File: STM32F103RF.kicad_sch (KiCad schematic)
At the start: 57 parts, among them J1 USB_A, J4 Conn_Coaxial, U1 SPX3819M5-L-3-3, U2 STM32F103C6Tx, U3 NRF24L01, Y1 16MHz, Y2 16MHz

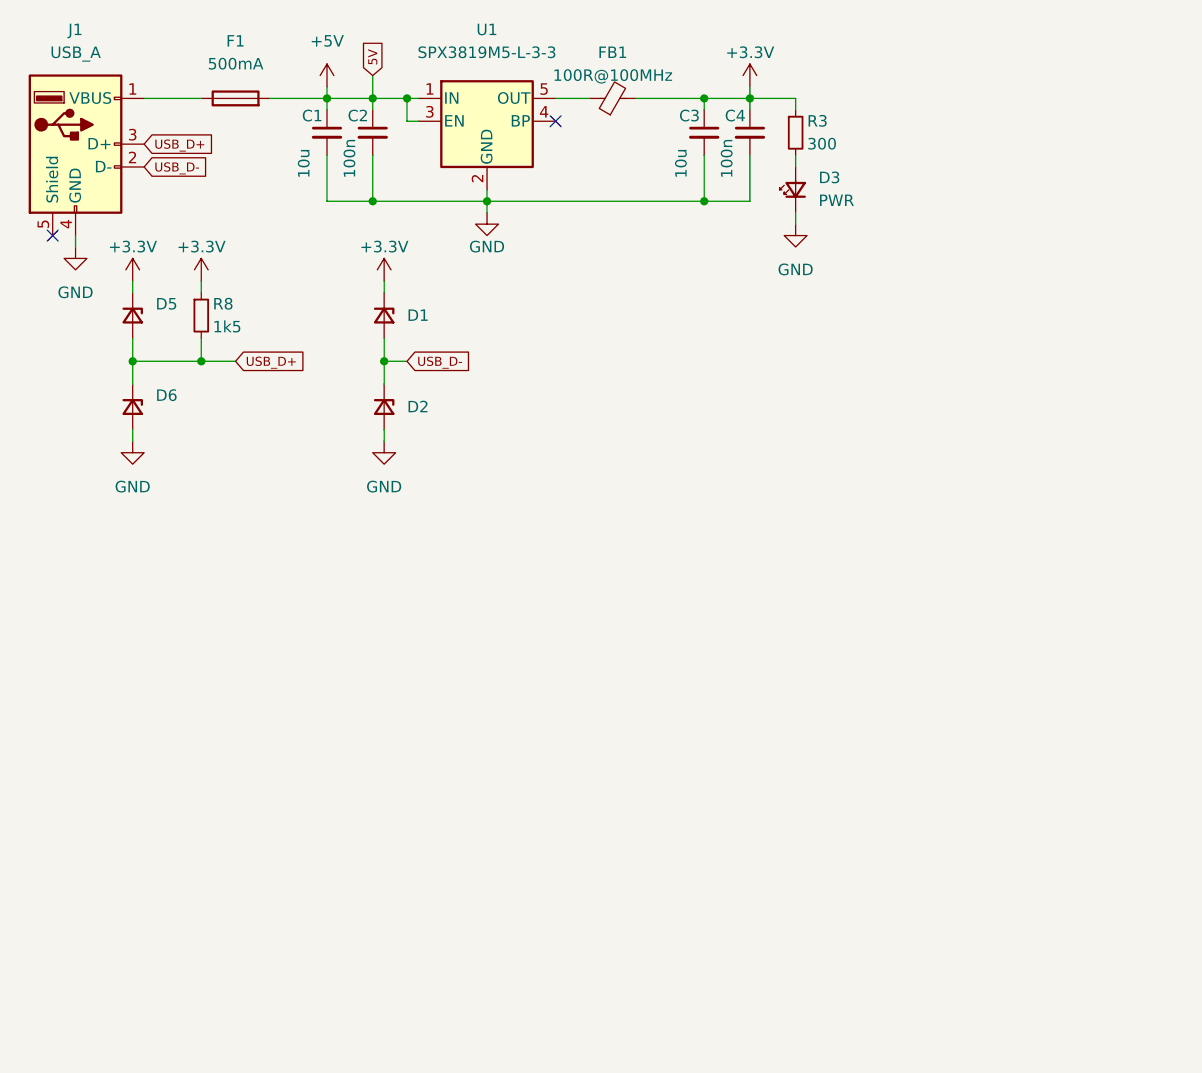
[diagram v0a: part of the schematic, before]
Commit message: Added usbc
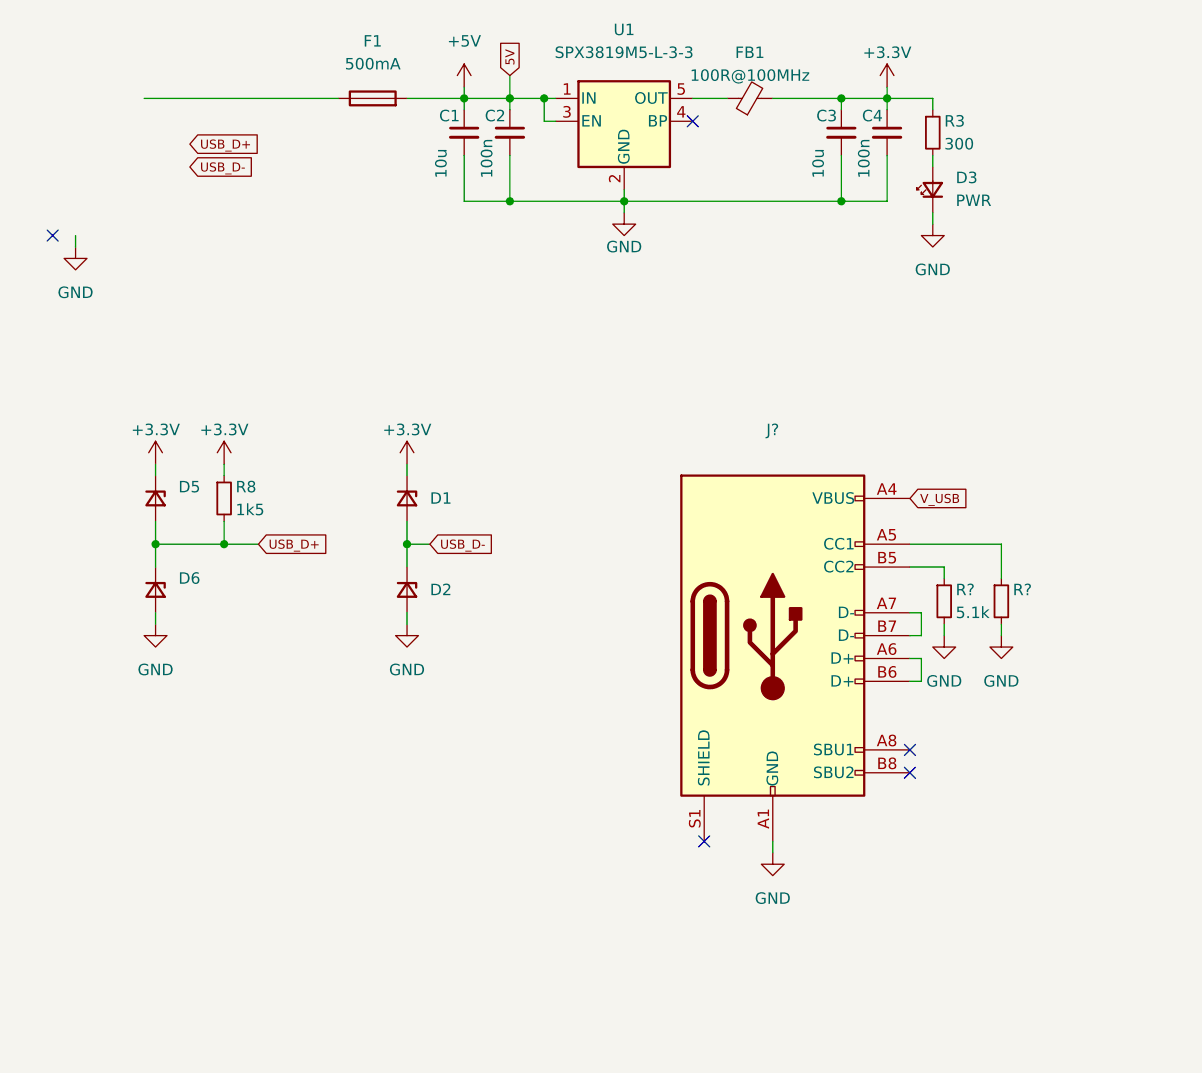
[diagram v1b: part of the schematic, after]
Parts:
- removed J1: USB_A, Connector_USB:USB_A_CNCTech_1001-011-01101_Horizontal, symbol Connector:USB_A
- added J?: (no value), symbol Connector:USB_C_Receptacle_USB2.0
- added R?: 5.1k, Resistor_SMD:R_0603_1608Metric_Pad0.98x0.95mm_HandSolder, symbol Device:R_Small
- added R?: (no value), symbol Device:R_Small
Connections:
- net GND: now also J?.A1 (GND), J?.A12 (GND), J?.B1 (GND), J?.B12 (GND), R?.2, R?.2
- new net: J?.B5 (CC2), R?.1
- new net: J?.A5 (CC1), R?.1
- new net: J?.A6 (D+), J?.B6 (D+)
- new net: J?.A7 (D-), J?.B7 (D-)
- new net V_USB: J?.A4 (VBUS), J?.A9 (VBUS), J?.B4 (VBUS), J?.B9 (VBUS)
- no-connect marks 2 -> 5
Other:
- moved on the sheet: C1, C2, C3, C4, D1, D2, D3, D5, D6, F1, FB1, R3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

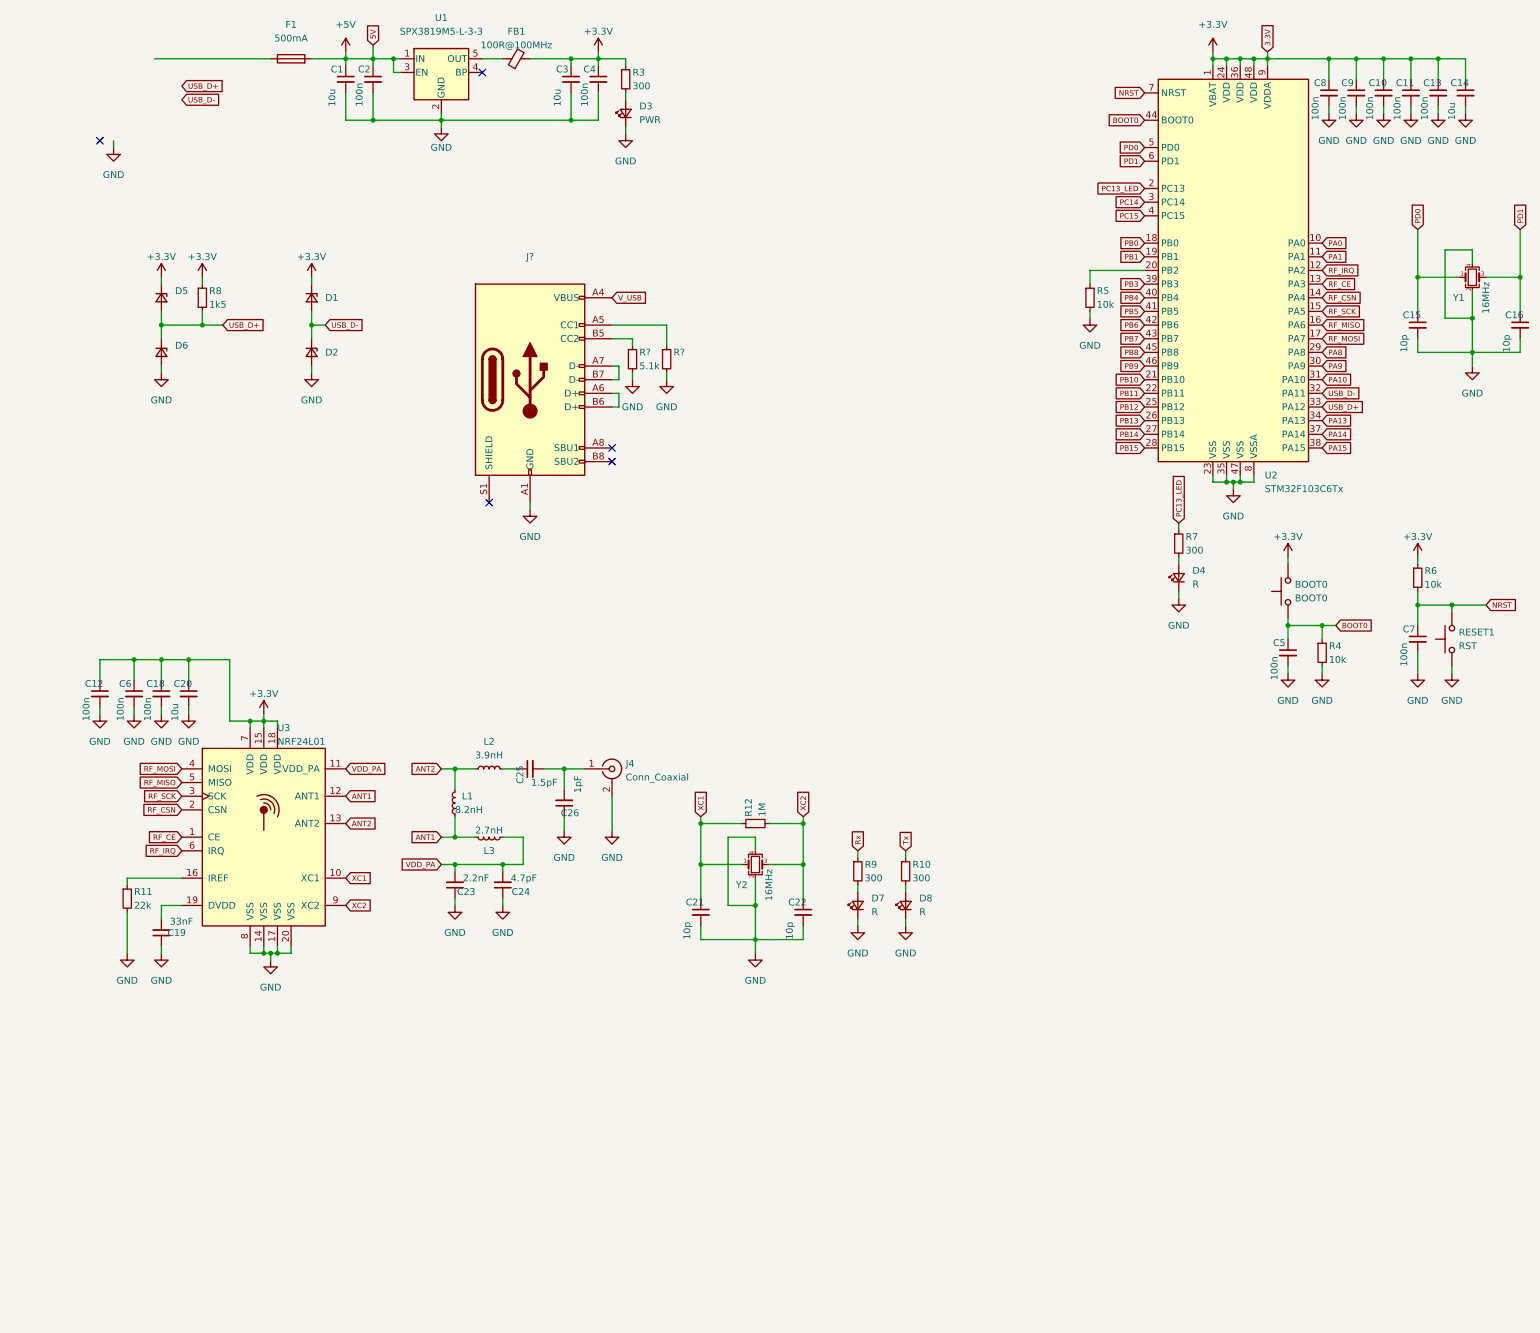
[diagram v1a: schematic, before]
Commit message: placing usb components
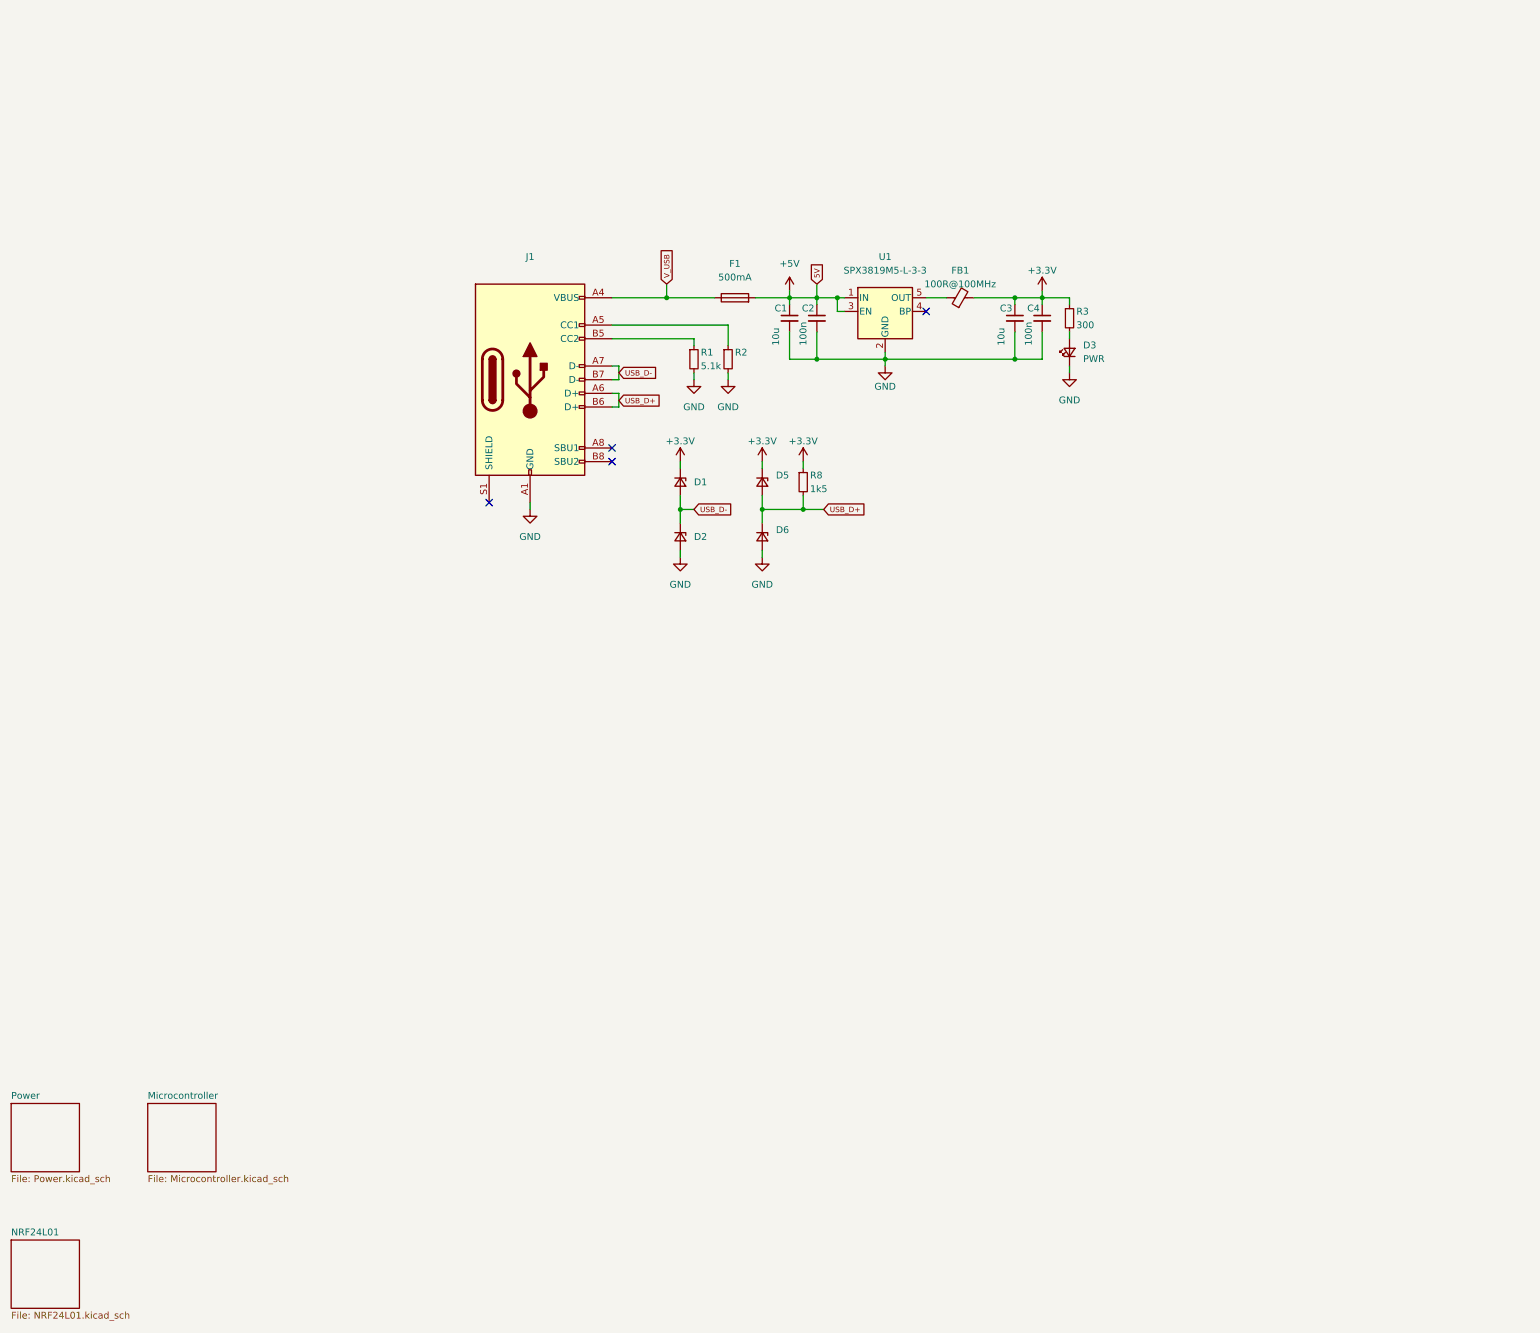
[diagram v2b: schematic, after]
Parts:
- removed BOOT0: BOOT0, Button_Switch_THT:SW_PUSH_6mm, symbol Switch:SW_Push
- removed C10, C11, C12, C13, C18, C5, C6, C7, C8, C9: 100n, Capacitor_SMD:C_0603_1608Metric_Pad1.08x0.95mm_HandSolder, symbol Device:C_Small
- removed C14, C20: 10u, Capacitor_SMD:C_0603_1608Metric_Pad1.08x0.95mm_HandSolder, symbol Device:C_Small
- removed C15, C16, C21, C22: 10p, Capacitor_SMD:C_0603_1608Metric_Pad1.08x0.95mm_HandSolder, symbol Device:C_Small
- removed C19: 33nF, Capacitor_SMD:C_0603_1608Metric_Pad1.08x0.95mm_HandSolder, symbol Device:C_Small
- removed C23: 2.2nF, Capacitor_SMD:C_0603_1608Metric_Pad1.08x0.95mm_HandSolder, symbol Device:C_Small
- removed C24: 4.7pF, Capacitor_SMD:C_0603_1608Metric_Pad1.08x0.95mm_HandSolder, symbol Device:C_Small
- removed C25: 1.5pF, Capacitor_SMD:C_0603_1608Metric_Pad1.08x0.95mm_HandSolder, symbol Device:C_Small
- removed C26: 1pF, Capacitor_SMD:C_0603_1608Metric_Pad1.08x0.95mm_HandSolder, symbol Device:C_Small
- removed D4, D7, D8: R, LED_SMD:LED_0603_1608Metric_Pad1.05x0.95mm_HandSolder, symbol Device:LED_Small
- removed J4: Conn_Coaxial, Connector_Coaxial:SMA_Amphenol_132289_EdgeMount, symbol Connector:Conn_Coaxial
- removed L1: 8.2nH, Inductor_SMD:L_0603_1608Metric_Pad1.05x0.95mm_HandSolder, symbol Device:L_Small
- removed L2: 3.9nH, Inductor_SMD:L_0603_1608Metric_Pad1.05x0.95mm_HandSolder, symbol Device:L_Small
- removed L3: 2.7nH, Inductor_SMD:L_0603_1608Metric_Pad1.05x0.95mm_HandSolder, symbol Device:L_Small
- removed R10, R7, R9: 300, Resistor_SMD:R_0603_1608Metric_Pad0.98x0.95mm_HandSolder, symbol Device:R_Small
- removed R11: 22k, Resistor_SMD:R_0603_1608Metric_Pad0.98x0.95mm_HandSolder, symbol Device:R_Small
- removed R12: 1M, Resistor_SMD:R_0603_1608Metric_Pad0.98x0.95mm_HandSolder, symbol Device:R_Small
- removed R4, R5, R6: 10k, Resistor_SMD:R_0603_1608Metric_Pad0.98x0.95mm_HandSolder, symbol Device:R_Small
- removed RESET1: RST, Button_Switch_THT:SW_PUSH_6mm, symbol Switch:SW_Push
- removed U2: STM32F103C6Tx, Package_QFP:LQFP-48_7x7mm_P0.5mm, symbol MCU_ST_STM32F1:STM32F103C6Tx
- removed U3: NRF24L01, Package_DFN_QFN:QFN-20-1EP_4x4mm_P0.5mm_EP2.5x2.5mm, symbol RF:NRF24L01
- removed Y1, Y2: 16MHz, Crystal:Crystal_SMD_2520-4Pin_2.5x2.0mm, symbol Device:Crystal_GND24_Small
- gave numbers to parts that had none: 3
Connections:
- net USB_D+: now also J1.A6 (D+), J1.B6 (D+)
- net USB_D-: now also J1.A7 (D-), J1.B7 (D-)
- net V_USB: now also F1.1
- no-connect marks 5 -> 4
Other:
- added sheet Microcontroller (Microcontroller.kicad_sch)
- added sheet NRF24L01 (NRF24L01.kicad_sch)
- added sheet Power (Power.kicad_sch)
- moved on the sheet: C1, C2, C3, C4, D1, D2, D3, D5, D6, F1, FB1, R1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

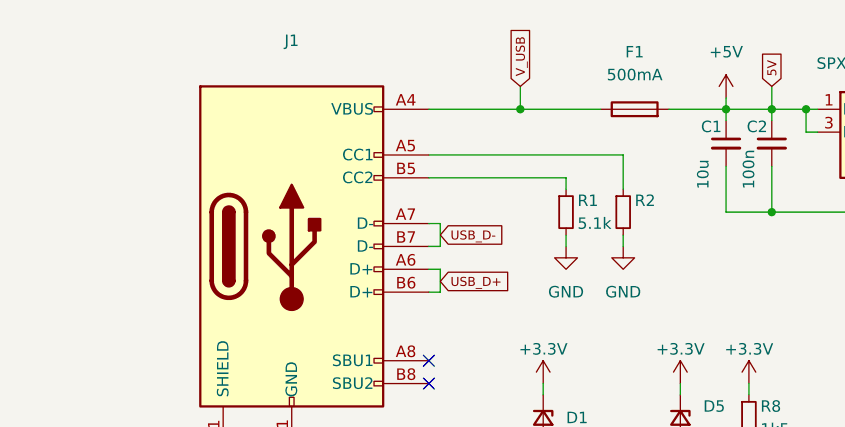
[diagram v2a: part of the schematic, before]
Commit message: 4-layer stackup & some rough component placement
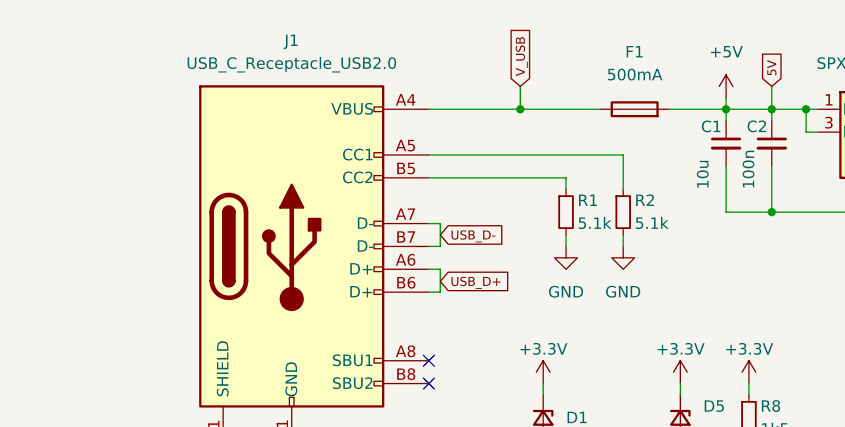
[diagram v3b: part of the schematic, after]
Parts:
- J1: value (none) -> USB_C_Receptacle_USB2.0; footprint (none) -> Connector_USB:USB_C_Receptacle_HRO_TYPE-C-31-M-12
- R2: value (none) -> 5.1k; footprint (none) -> Resistor_SMD:R_0603_1608Metric_Pad0.98x0.95mm_HandSolder
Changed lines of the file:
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@@
       (effects (font (size 1.27 1.27)) (justify left))
     )
-    (property "Value" "" (id 1) (at 134.62 78.74 0)
+    (property "Value" "5.1k" (id 1) (at 134.62 78.74 0)
       (effects (font (size 1.27 1.27)) (justify left))
     )
-    (property "Footprint" "" (id 2) (at 133.35 77.47 0)
+    (property "Footprint" "Resistor_SMD:R_0603_1608Metric_Pad0.98x0.95mm_HandSolder" (id 2) (at 133.35 77.47 0)
       (effects (font (size 1.27 1.27)) hide)
     )
@@
     (in_bom yes) (on_board yes) (fields_autoplaced)
     (property "Reference" "J1" (id 0) (at 96.52 58.42 0))
-    (property "Value" "" (id 1) (at 96.52 60.96 0))
-    (property "Footprint" "" (id 2) (at 100.33 81.28 0)
+    (property "Value" "USB_C_Receptacle_USB2.0" (id 1) (at 96.52 60.96 0))
+    (property "Footprint" "Connector_USB:USB_C_Receptacle_HRO_TYPE-C-31-M-12" (id 2) (at 100.33 81.28 0)
       (effects (font (size 1.27 1.27)) hide)
     )

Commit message: sum layouting
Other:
- removed sheet Power
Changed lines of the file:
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@@
     (pin "2")
   )
-  (sheet (at 25.4 215.9) (size 12.7 12.7) (fields_autoplaced)
+  (sheet (at 0 215.9) (size 12.7 12.7) (fields_autoplaced)
     (stroke (width 0.1524) (type solid) (color 0 0 0 0))
     (fill (color 0 0 0 0.0000))
-    (property "Sheet name" "Microcontroller" (id 0) (at 25.4 215.1884 0)
+    (property "Sheet name" "Microcontroller" (id 0) (at 0 215.1884 0)
       (effects (font (size 1.27 1.27)) (justify left bottom))
     )
-    (property "Sheet file" "Microcontroller.kicad_sch" (id 1) (at 25.4 229.1846 0)
+    (property "Sheet file" "Microcontroller.kicad_sch" (id 1) (at 0 229.1846 0)
       (effects (font (size 1.27 1.27)) (justify left top))
     )
@@
     )
   )
-  (sheet (at 0 215.9) (size 12.7 12.7) (fields_autoplaced)
-    (stroke (width 0.1524) (type solid) (color 0 0 0 0))
-    (fill (color 0 0 0 0.0000))
-    (property "Sheet name" "Power" (id 0) (at 0 215.1884 0)
-      (effects (font (size 1.27 1.27)) (justify left bottom))
-    )
-    (property "Sheet file" "Power.kicad_sch" (id 1) (at 0 229.1846 0)
-      (effects (font (size 1.27 1.27)) (justify left top))
-    )
-  )
   (sheet_instances
     (path "/" (page "1"))
-    (path "/e695916d-aeac-47da-bd39-0c77c38bea8d" (page "2"))
     (path "/3b596506-65bf-4a2a-90c0-c8e397dd346e" (page "3"))
     (path "/e3a54d70-49a5-419a-b99e-e9f481ea3702" (page "4"))
@@
       (reference "#PWR0126") (unit 1) (value "GND") (footprint "")
     )
-    (path "/3b596506-65bf-4a2a-90c0-c8e397dd346e/7dc61b8f-c79a-4b32-a44c-9031797cd123"
-      (reference "#PWR0127") (unit 1) (value "GND") (footprint "")
-    )
     (path "/6f45cbc5-3083-4691-b395-c12aececd83d"
       (reference "#PWR0128") (unit 1) (value "GND") (footprint "")
@@
       (reference "R11") (unit 1) (value "1M") (footprint "Resistor_SMD:R_0603_1608Metric_Pad0.98x0.95mm_HandSolder")
     )
-    (path "/3b596506-65bf-4a2a-90c0-c8e397dd346e/ae6018fa-0784-4a92-8e2f-b97f4144db6c"
-      (reference "RESET1") (unit 1) (value "RST") (footprint "Button_Switch_THT:SW_PUSH_6mm")
-    )
     (path "/c6b070fb-230d-42f9-b182-7a55fca635e2"
